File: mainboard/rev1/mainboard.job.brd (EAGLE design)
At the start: 40.6 x 30.5 mm, 82 parts, among them Q1 MOSFET-NCHANNEL2N7002PW, Q2 MOSFET-NCHANNEL2N7002PW, Q3 MOSFET-NCHANNEL2N7002PW, Q4 BSS84, Q5 BSS84, Q6 MOSFET-NCHANNEL2N7002PW, Q7 MOSFET-NCHANNEL2N7002PW, X1 CRYSTAL"32.768"

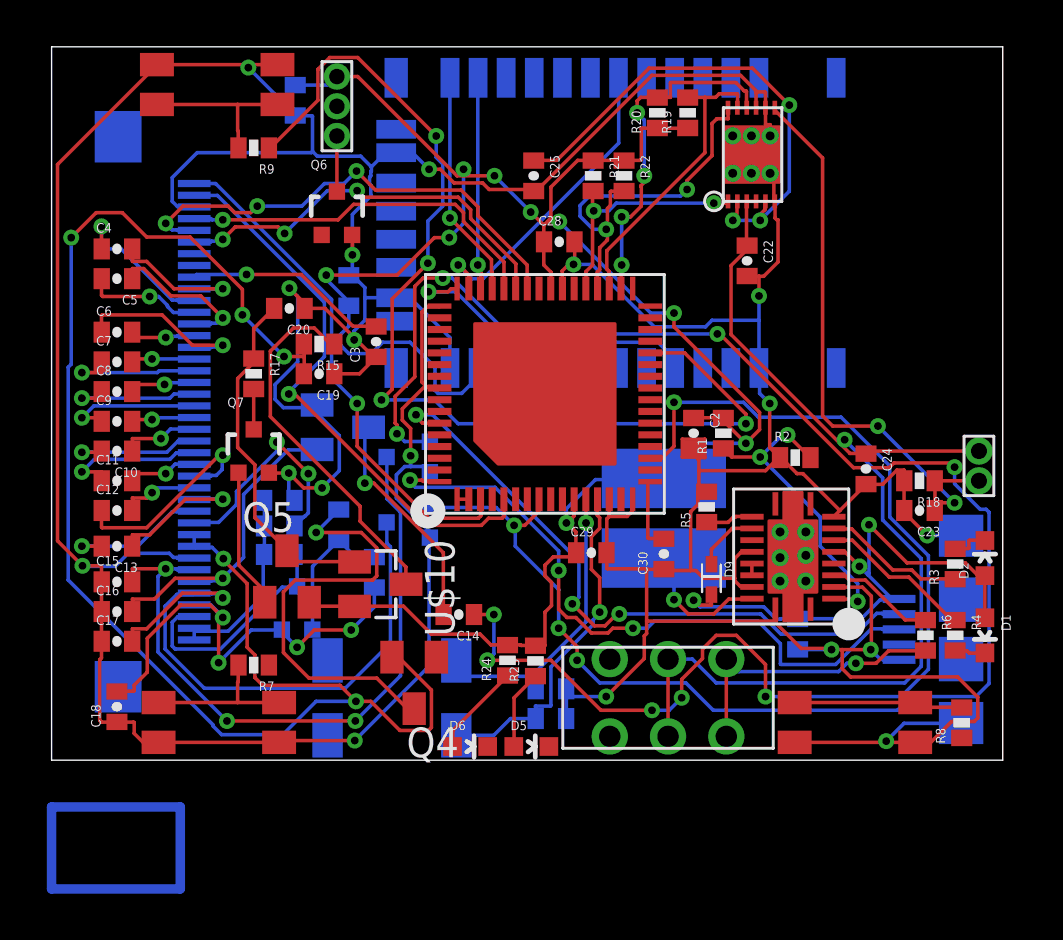
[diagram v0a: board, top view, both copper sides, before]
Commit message: updated schematic for rev1
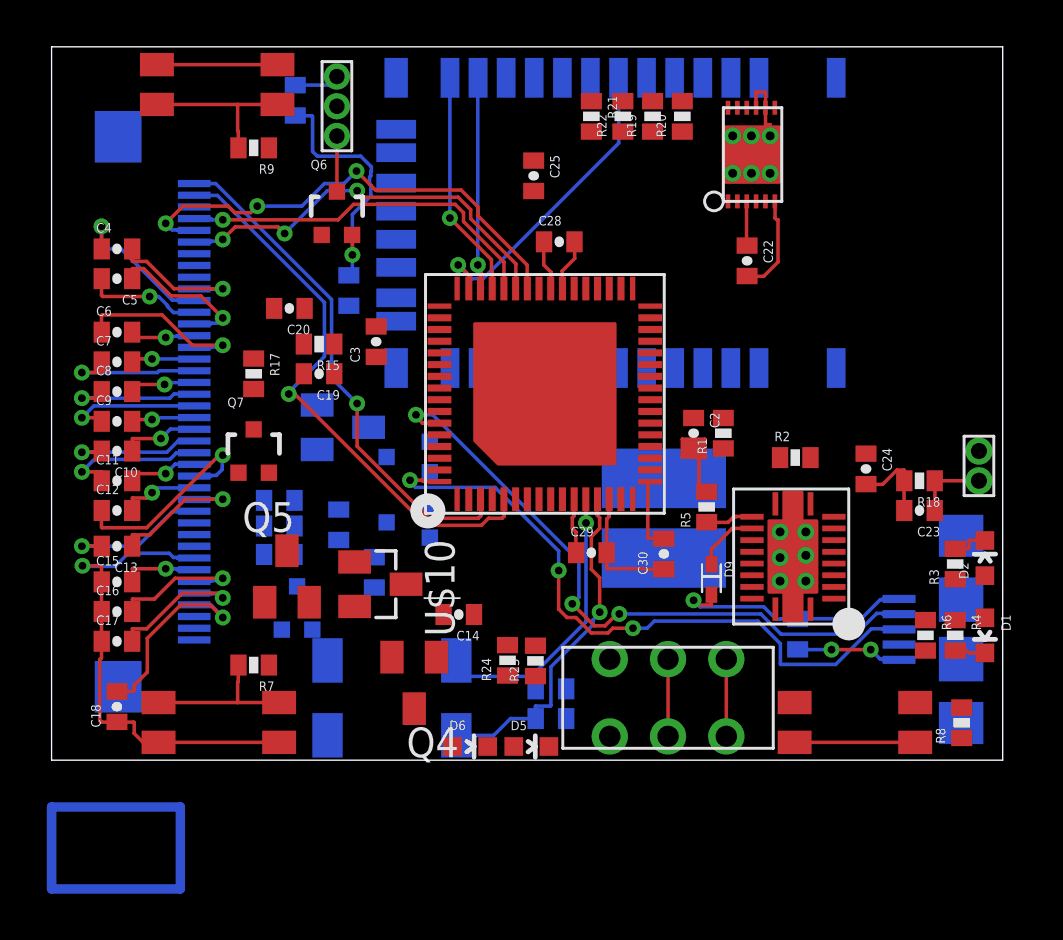
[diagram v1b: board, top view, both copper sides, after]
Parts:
- moved R21 2.54 mm to (23.1, 27.5)
- moved R22 2.54 mm to (24.4, 27.5), turned to 90 degrees
- moved R19 1.51 mm to (25.7, 27.5)
- moved R20 1.08 mm to (26.9, 27.5)
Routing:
- net GND: track 269.1 -> 71.4 mm, vias 18 -> 4
- net VCC: track 92.7 -> 6.67 mm, vias 9 -> 0
- net EPD_DISCHARGE: track 76.6 -> 0.00 mm, vias 7 -> 0
- net VCC_T: track 65.2 -> 0.00 mm, vias 5 -> 0
- net EPD_PWM: track 49.9 -> 0.00 mm, vias 6 -> 0
- net BTN_2: track 45.0 -> 0.00 mm, vias 4 -> 0
- net BATT_PWR: track 45.8 -> 5.24 mm, vias 1 -> 0
- net VGH: track 28.9 -> 3.24 mm, vias 3 -> 1
- net PM_SRP: track 25.5 -> 3.18 mm, vias 2 -> 0
- net VCC_R: track 21.6 -> 0.00 mm, vias 3 -> 0
- net VDH: track 26.1 -> 6.42 mm
- net N$8: track 18.9 -> 0.00 mm, vias 1 -> 0
- net PM_GPOUT: track 16.2 -> 0.00 mm, vias 2 -> 0
- net N$47: track 15.8 -> 0.00 mm
- net PM_SDA: track 15.0 -> 0.00 mm, vias 4 -> 0
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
